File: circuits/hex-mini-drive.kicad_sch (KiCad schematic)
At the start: 66 parts, among them CN5 Conn_01x08_Pin

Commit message: Tentatively complete the PCB layout.
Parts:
- removed C10, C11, C12, C13, C20, C21, C22, C8: 0.1uF, components_footprints:C0805, symbol components_schematics:CC0805KRX7R9BB104
- removed C6, C7, C9: 1uF, components_footprints:C0805, symbol components_schematics:CL21B105KBFNNNE
- removed CN1, CN2: ~, components_footprints:FPC-SMD_KH-FG1.0-H2.0-8PIN, symbol components_schematics:KH-FG1.0-H2.0-8PIN
- removed CN5: Conn_01x08_Pin, components_footprints:PinHeader_1x08_P1.27mm_Vertical, symbol components_schematics:Conn_01x08_Pin
- removed R15, R16, R17, R18, R19: 10Ω, ProLibrary_pcs_2024-06-22:R0603, symbol components_schematics:0603WAF100JT5E
- added C10, C11, C12, C13, C20, C21, C22, C8: 100nF, components_footprints:C0603, symbol components_schematics:CC0603KRX7R9BB104
- added C23: 10uF, components_footprints:C1206, symbol components_schematics:CL31A106KBHNNNE
- added C6, C7, C9: 1uF, components_footprints:C0603, symbol components_schematics:CL10A105KB8NNNC
- added CN1, CN2: ~, components_footprints:FPC-SMD_P0.50-16P_FGS-XJ-H2.0, symbol components_schematics:AFC01-S16FCA-00
- C18, C19: footprint ProLibrary_pcs_2024-06-22 (5):C0603 -> components_footprints:C0603
- R10, R5, R6, R7, R8, R9: footprint ProLibrary_pcs_2024-06-22:R0603 -> components_footprints:R0603
- R11, R12, R13, R14: footprint ProLibrary_pcs_2024-06-22 (4):R0603 -> components_footprints:R0603
- R20: footprint ProLibrary_pcs_2024-06-05 (14):R0603 -> components_footprints:R0603
- U4: footprint components_footprints:SOT-223-3_L6.5-W3.4-P2.30-LS7.0-BR -> components_footprints:AMS1117-3.3 SOT-223-3_L6.5-W3.4-P2.30-LS7.0-BR
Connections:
- net TIM2_CH1 is gone; now on net TIM2_CH1/H1: U1.10 (PA0-WKUP)
- net TIM2_CH2 is gone; now on net TIM2_CH2/H2: U1.11 (PA1)
- net TIM2_CH3 is gone; now on net TIM2_CH3/H3: U1.21 (PB10)
- net +3V3: now also C10.2, C11.2, C12.2, C13.2, C22.2, C6.2, CN2.1
- net +3V3A: now also C8.2, C9.2
- net +5V: now also CN1.1, CN2.16
- net +VDC: now also C23.1, CN1.12, CN1.13, CN1.14, CN1.15, CN1.16
- net ADC1_IN5/REF: now also C21.2
- net BOOT0: now also CN1.5
- net GND: now also C10.1, C11.1, C12.1, C13.1, C20.1, C21.1, C22.1, C23.2, C6.1, C7.1, C8.1, C9.1, CN1.10, CN1.11, CN1.7, CN1.8, CN1.9, CN2.2
- net GPIO_Input_A: now also CN2.9
- net GPIO_Input_B: now also CN2.10
- net GPIO_Input_C: now also CN2.11
- net GPIO_Input_CS: now also CN1.4
- net I2C1_SCL: now also CN2.4
- net I2C1_SDA: now also CN2.3
- net SPI2MISO: now also CN2.6
- net SPI2_MOSI: now also CN2.5
- net SPI2_NSS: now also CN2.8
- net SPI2_SCK: now also CN2.7
- net SYS_JTCK-SWCLK: now also CN2.13
- net SYS_JTDI: now also CN2.14
- net SYS_JTDO-TRACESWO: now also CN2.15
- net SYS_JTMS-SWDIO: now also CN2.12
- net USART1_RX: now also CN1.3
- net USART1_TX: now also CN1.2
- net LO3: now reaches R8.2, U3.9 (LO3)
- net HO1: now reaches R5.1, U3.19 (HO1)
- net LO1: now reaches R6.1, U3.11 (LO1)
- net NRST: now reaches U1.7 (NRST)
- net NRST: now also C20.2, CN1.6
- net Filtered +5V: now reaches L1.1, U4.3 (VIN)
- net Filtered +5V: now also C7.2
- net LO2: now reaches R7.2, U3.10 (LO2)
- net Boost Gate 3: now reaches C3.2, D3.1 (K), U3.14 (VB3)
- net HO3: now reaches R10.1, U3.13 (HO3)
- net HO2: now reaches R9.1, U3.16 (HO2)
- net Boost Gate 2: now reaches C2.2, D2.1 (K), U3.17 (VB2)
- net Boost Gate 1: now reaches C1.2, D1.1 (K), U3.20 (VB1)
- net H1 renamed TIM2_CH1/H1
- net H2 renamed TIM2_CH2/H2
- net H3 renamed TIM2_CH3/H3
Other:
- note removed: "Add signal dampening between hall sensors and MCU inputs."
- note removed: "Connect boot with the CS line, because we can't read the boot pin after wakeup."
- note removed: "Debug and spare pins."
- moved on the sheet: C14, C15, C16, C17, C18, C19, CN3, CN4, R10, R5, R6, R7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

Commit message: Finalise mini drive test circuit and generate production files.
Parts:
- C1, C2, C3: LCSC Part # (none) -> C1710
- C10, C11, C12, C13, C20, C21, C22, C8: LCSC Part # (none) -> C14663
- C14, C15, C16, C17, C23, C5: LCSC Part # (none) -> C13585
- C18, C19: LCSC Part # (none) -> C1658
- C4: LCSC Part # (none) -> C49678
- C6, C7, C9: LCSC Part # (none) -> C15849
- CN1, CN2: LCSC Part # (none) -> C262665
- CN3: LCSC Part # (none) -> C9139
- CN4: LCSC Part # (none) -> C5160305
- D1, D2, D3: LCSC Part # (none) -> C2128
- L1: LCSC Part # (none) -> C1017
- L2: LCSC Part # (none) -> C1046
- LED1: LCSC Part # (none) -> C965840
- Q1, Q2, Q3, Q4, Q5, Q6: LCSC Part # (none) -> C358681
- R1, R2, R3: LCSC Part # (none) -> C163089
- R10, R5, R6, R7, R8, R9: LCSC Part # (none) -> C22859
- R11, R12, R13, R14: LCSC Part # (none) -> C22843
- R20: LCSC Part # (none) -> C25804
- R21, R22: LCSC Part # (none) -> C25819
- R4: LCSC Part # (none) -> C25803
- U1: LCSC Part # (none) -> C8734
- U2: LCSC Part # (none) -> C2058366
- U3: LCSC Part # (none) -> C5804616
- U4: LCSC Part # (none) -> C6186
- X1: LCSC Part # (none) -> C115962

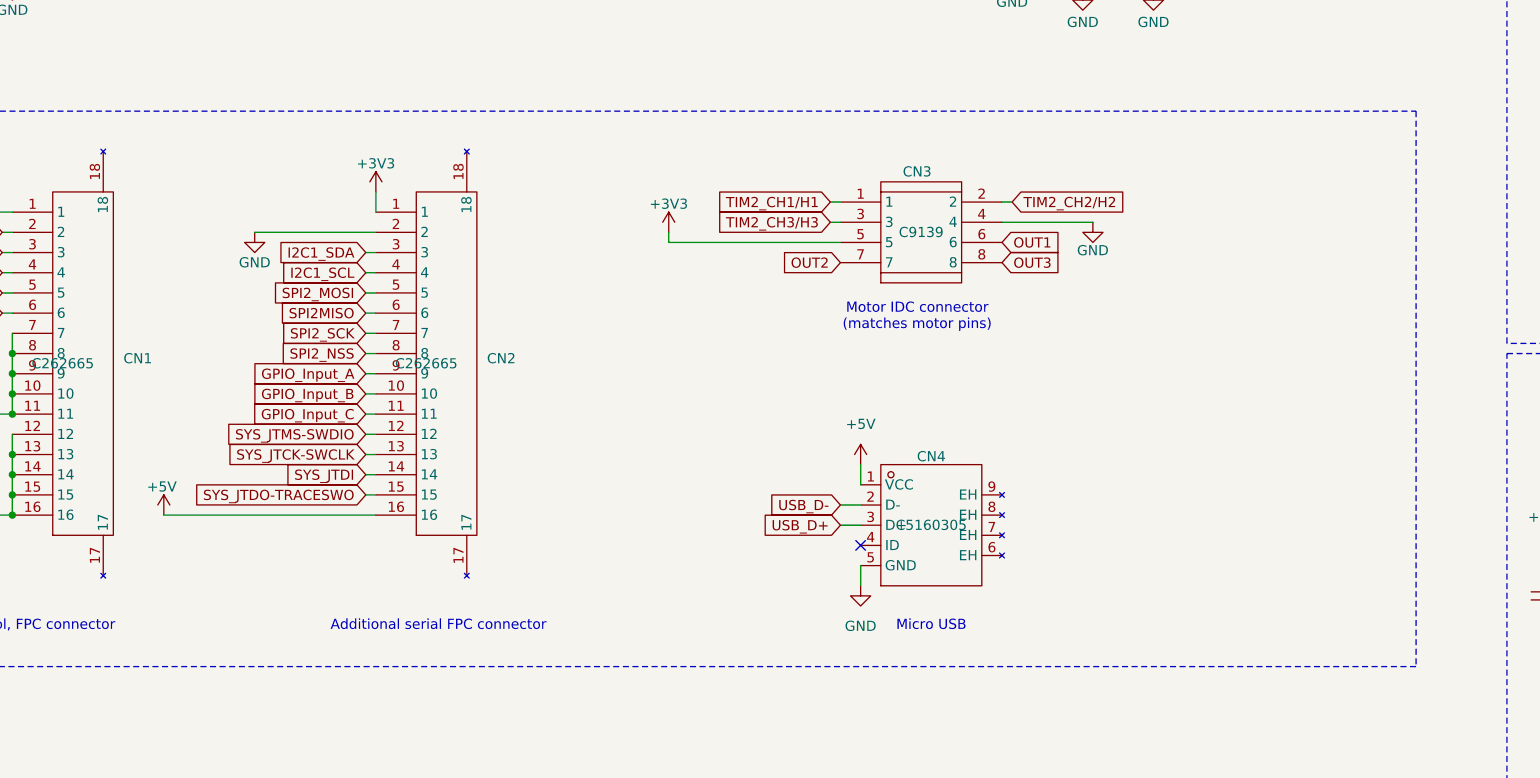
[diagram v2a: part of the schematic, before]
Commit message: Redo design with minimum 0.2mm line width and spacing.
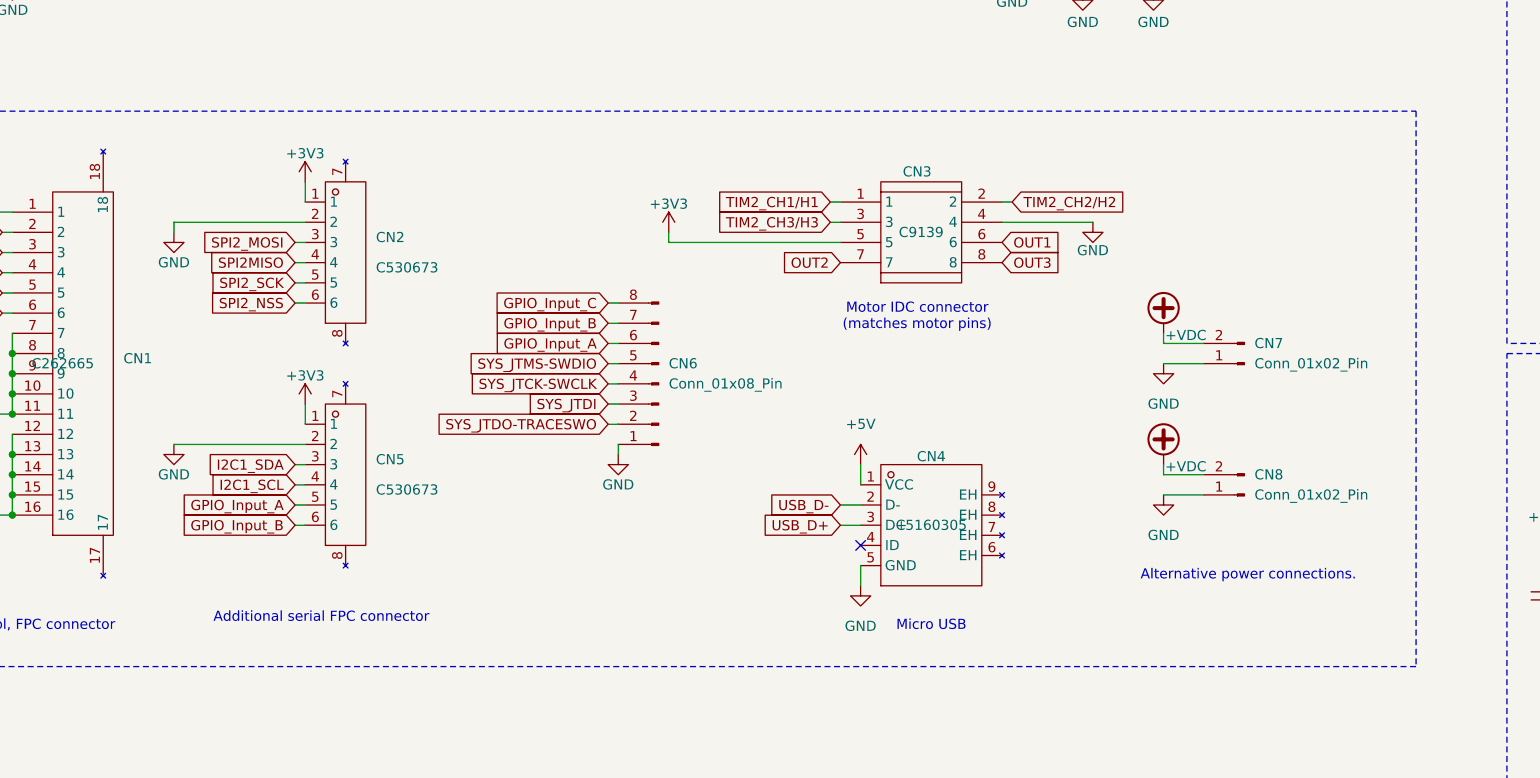
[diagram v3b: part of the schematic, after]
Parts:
- removed CN2: ~, components_footprints:FPC-SMD_P0.50-16P_FGS-XJ-H2.0, symbol components_schematics:AFC01-S16FCA-00
- added CN2, CN5: ~, components_footprints:FPC-SMD_6P-P0.50_L3.8-W5.0, symbol components_schematics:KH-0.5-H3.25-6PIN
- added CN6: Conn_01x08_Pin, components_footprints:PinHeader_1x08_P1.00mm_Vertical, symbol components_schematics:Conn_01x08_Pin
- added CN7, CN8: Conn_01x02_Pin, components_footprints:PinHeader_1x02_P2.00mm_Vertical, symbol components_schematics:Conn_01x02_Pin
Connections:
- net +3V3: now also CN2.1, CN5.1
- net +VDC: now also CN7.2 (Pin_2), CN8.2 (Pin_2)
- net GND: now also CN2.2, CN5.2, CN6.1 (Pin_1), CN7.1 (Pin_1), CN8.1 (Pin_1)
- net GPIO_Input_A: now also CN5.5, CN6.6 (Pin_6)
- net GPIO_Input_B: now also CN5.6, CN6.7 (Pin_7)
- net GPIO_Input_C: now also CN6.8 (Pin_8)
- net I2C1_SCL: now also CN5.4
- net I2C1_SDA: now also CN5.3
- net SPI2MISO: now also CN2.4
- net SPI2_MOSI: now also CN2.3
- net SPI2_NSS: now also CN2.6
- net SPI2_SCK: now also CN2.5
- net SYS_JTCK-SWCLK: now also CN6.4 (Pin_4)
- net SYS_JTDI: now also CN6.3 (Pin_3)
- net SYS_JTDO-TRACESWO: now also CN6.2 (Pin_2)
- net SYS_JTMS-SWDIO: now also CN6.5 (Pin_5)
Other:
- note added: "Alternative power connections."

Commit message: Update schematic information panel.
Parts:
- R20: value 10kΩ -> 10kΩ
- R21, R22: value 47kΩ -> 47kΩ
- R4: value 100kΩ -> 100kΩ
